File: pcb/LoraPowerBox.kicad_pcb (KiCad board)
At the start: 4 copper layers, 51.6 x 60.6 mm, 49 parts, among them J1 Conn_01x04_Pin, J10 Conn_01x02_Pin, J11 Conn_01x02_Pin, J12 Conn_01x05_Pin, J2 Conn_01x04_Pin, J3 Conn_01x04_Pin, J4 Conn_01x06_Pin, J5 Conn_01x04_Pin, J6 Conn_01x04_Pin, J7 Conn_01x04_Pin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

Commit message: pcb, sch: add resistor values for NTC voltage divider
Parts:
- R7: value R -> 5.23k
- R8: value R -> 30.1k
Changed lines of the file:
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@@
 			)
 		)
-		(property "Value" "R"
+		(property "Value" "5.23k"
 			(at 0 1.43 0)
 			(layer "F.Fab")
@@
 			)
 		)
-		(property "Value" "R"
+		(property "Value" "30.1k"
 			(at 0 1.43 0)
 			(layer "F.Fab")

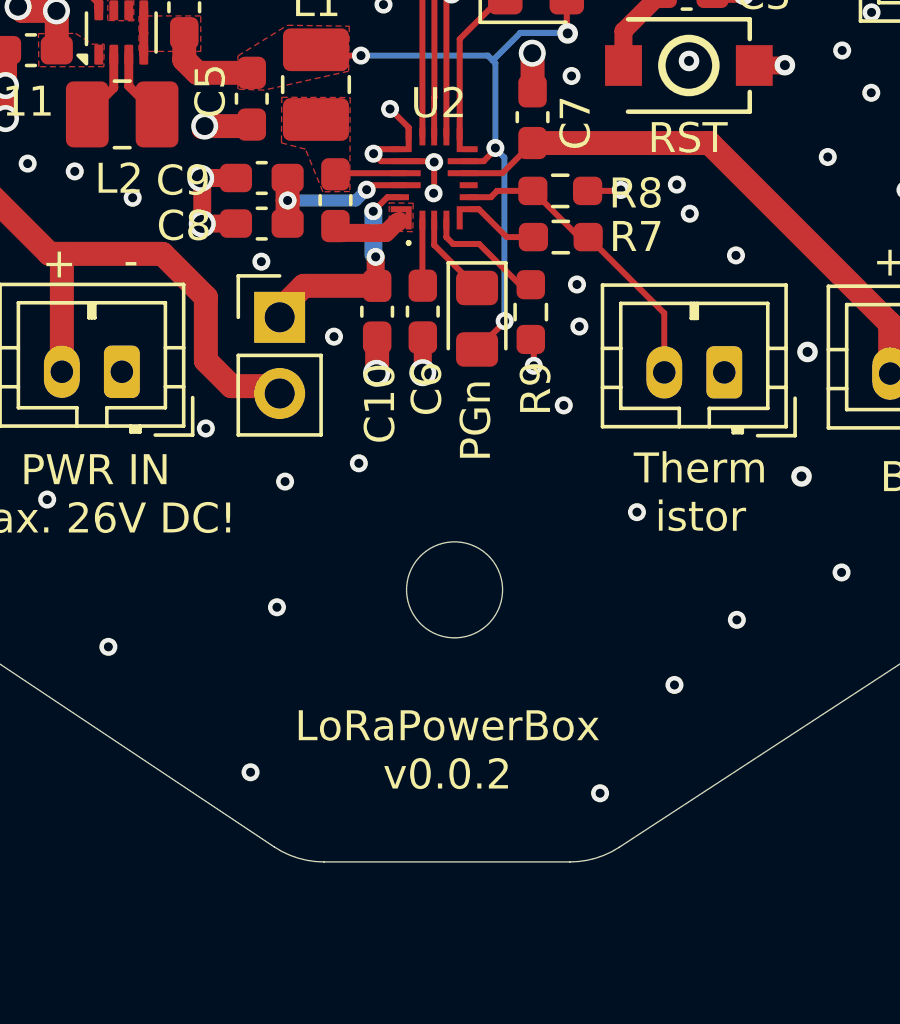
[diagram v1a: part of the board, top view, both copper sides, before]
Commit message: pcb, sch: replace M3 hounting hole with M4
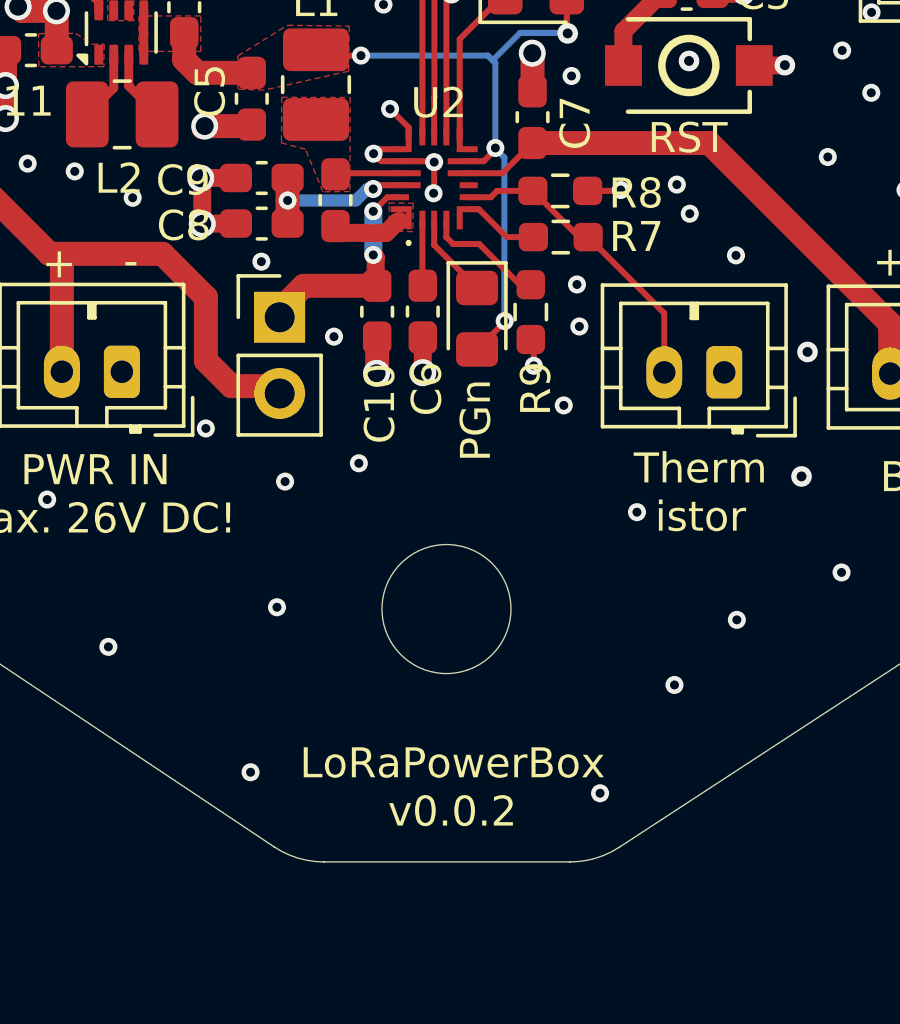
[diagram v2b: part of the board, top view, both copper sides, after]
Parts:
- H1: footprint MountingHole:MountingHole_3.2mm_M3 -> MountingHole:MountingHole_4.3mm_M4_DIN965
- moved H1 0.69 mm to (137.5, 91.6)
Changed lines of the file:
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@@
 		)
 	)
-	(footprint "MountingHole:MountingHole_3.2mm_M3"
+	(footprint "MountingHole:MountingHole_4.3mm_M4_DIN965"
 		(layer "F.Cu")
-		(at 137.76 90.93)
-		(descr "Mounting Hole 3.2mm, M3, no annular, generated by kicad-footprint-generator mountinghole.py")
-		(tags "mountinghole M3")
+		(at 137.49 91.57)
+		(descr "Mounting Hole 4.3mm, M4, no annular, generated by kicad-footprint-generator mountinghole.py")
+		(tags "mountinghole M4 DIN965")
 		(property "Reference" "H1"
-			(at 0 -4.15 0)
+			(at 0 -4.7 0)
 			(layer "F.SilkS")
 			(hide yes)
@@
 		)
 		(property "Value" "MountingHole"
-			(at 0 4.15 0)
+			(at 0 4.7 0)
 			(layer "F.Fab")
 			(hide yes)
@@
 		(fp_circle
 			(center 0 0)
-			(end 3.2 0)
+			(end 3.75 0)
 			(stroke
 				(width 0.15)
@@
 		(fp_circle
 			(center 0 0)
-			(end 3.45 0)
+			(end 4 0)
 			(stroke
 				(width 0.05)
@@
 		)
 		(fp_text user "${REFERENCE}"
-			(at -0.168654 0.2 0)
+			(at 0 0 0)
 			(layer "F.Fab")
 			(effects
@@
 		(pad "" np_thru_hole circle
 			(at 0 0)
-			(size 3.2 3.2)
-			(drill 3.2)
+			(size 4.3 4.3)
+			(drill 4.3)
 			(layers "*.Cu" "*.Mask")
 		)
@@
 	)
 	(gr_text "LoRaPowerBox\nv0.0.2\n"
-		(at 137.525 97.675 0)
+		(at 137.69 98.91 0)
 		(layer "F.SilkS")
 		(effects
@@
 	)
 	(segment
+		(start 135.04771 77.56825)
+		(end 135.17471 77.44125)
+		(width 0.2)
+		(layer "F.Cu")
+		(net 7)
+	)
+	(segment
 		(start 132.195 77.95125)
 		(end 132.195 77.20125)
@@
 	)
 	(segment
-		(start 134.83 77.59125)
-		(end 134.98 77.44125)
+		(start 135.17471 77.44125)
+		(end 136.13 77.44125)
 		(width 0.2)
 		(layer "F.Cu")
@@
 		(net 7)
 	)
-	(segment
-		(start 134.98 77.44125)
-		(end 136.13 77.44125)
-		(width 0.2)
-		(layer "F.Cu")
-		(net 7)
-	)
 	(via
 		(at 132.195 77.95125)
@@
 	)
 	(via
-		(at 134.83 77.59125)
+		(at 135.04771 77.56825)
 		(size 0.6)
 		(drill 0.3)
@@
 	)
 	(segment
-		(start 134.83 77.59125)
+		(start 135.04771 77.56825)
+		(end 134.853 77.56825)
+		(width 0.4)
+		(layer "B.Cu")
+		(net 7)
+	)
+	(segment
+		(start 134.853 77.56825)
 		(end 134.47 77.95125)
 		(width 0.4)
@@
 	)
 	(segment
-		(start 135.13 79.83125)
-		(end 135.13 80.74625)
-		(width 0.6)
-		(layer "F.Cu")
-		(net 9)
-	)
-	(segment
 		(start 132.73375 80.79625)
 		(end 131.93 81.6)
@@
 		(net 9)
 	)
+	(segment
+		(start 135.13 79.84625)
+		(end 135.13 80.74625)
+		(width 0.6)
+		(layer "F.Cu")
+		(net 9)
+	)
+	(segment
+		(start 135.05 79.76625)
+		(end 135.13 79.84625)
+		(width 0.6)
+		(layer "F.Cu")
+		(net 9)
+	)
 	(via
-		(at 135.13 79.83125)
+		(at 135.05 79.76625)
 		(size 0.6)
 		(drill 0.3)
@@
 	(segment
 		(start 135.05 79.75125)
-		(end 135.13 79.83125)
+		(end 135.05 79.76625)
 		(width 0.2)
 		(layer "B.Cu")

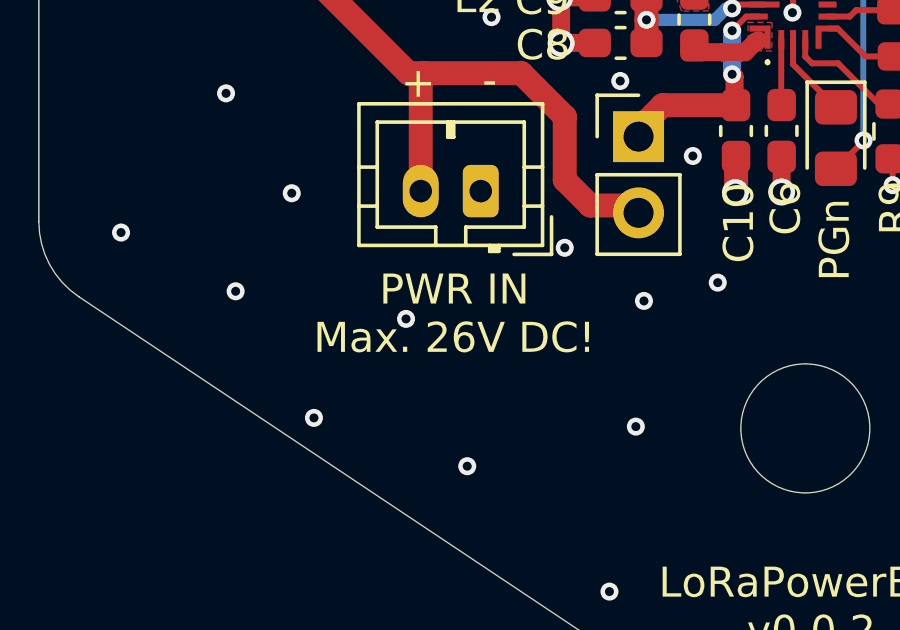
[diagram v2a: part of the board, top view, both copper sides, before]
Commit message: pcb: the internal ADC maxes out at 18V. So rework silk print regaring voltage limits
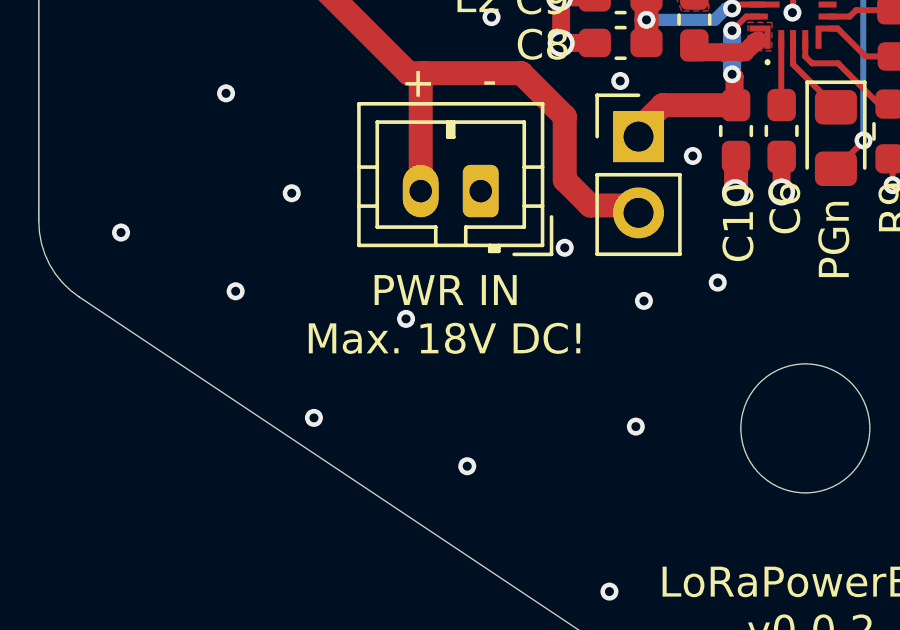
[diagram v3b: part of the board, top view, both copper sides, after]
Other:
- board text added: "PWR IN Max. 18V DC!"
- board text removed: "PWR IN Max. 26V DC!"
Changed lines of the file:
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@@
 		)
 	)
-	(gr_text "PWR IN\nMax. 26V DC!"
-		(at 125.79 89.14 0)
+	(gr_text "PWR IN\nMax. 18V DC!\n"
+		(at 125.5 89.19 0)
 		(layer "F.SilkS")
 		(effects

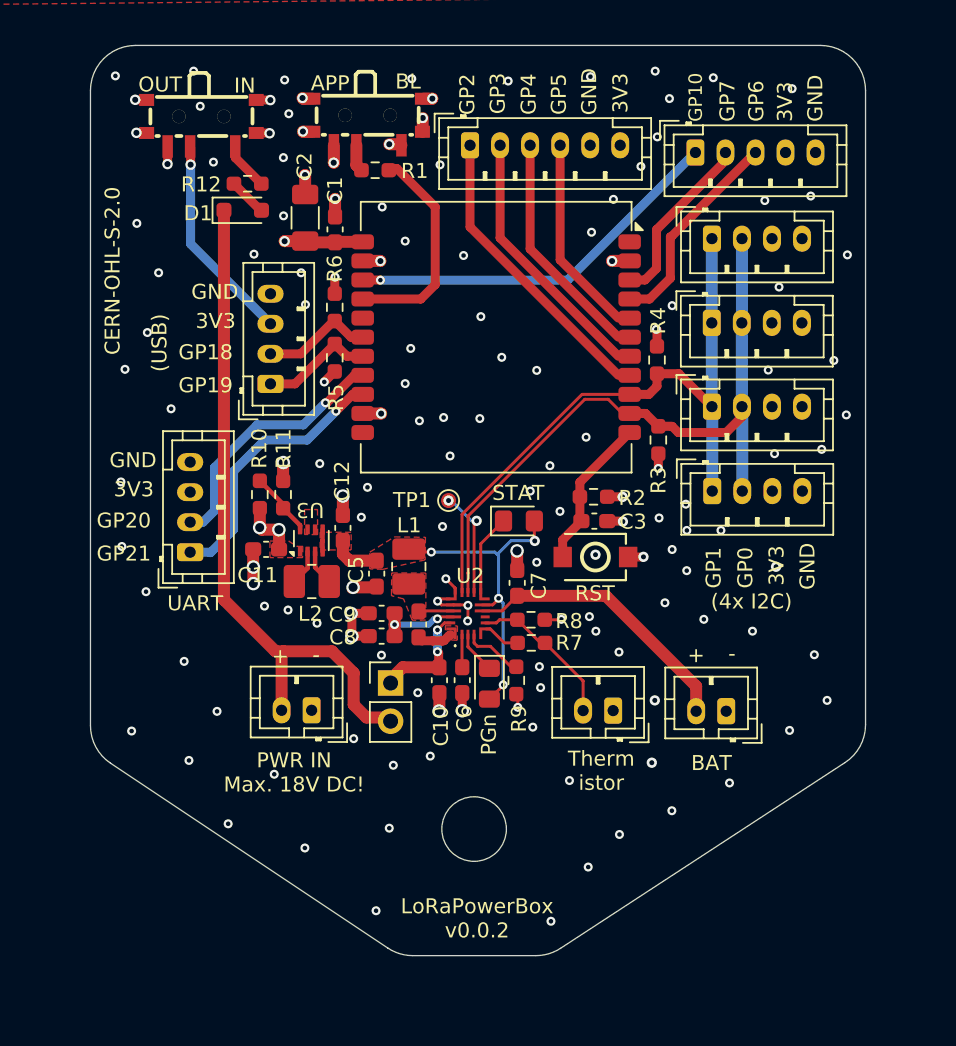
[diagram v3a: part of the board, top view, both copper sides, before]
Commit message: pcb: finally found the right kicad buttoms to center everything correctly
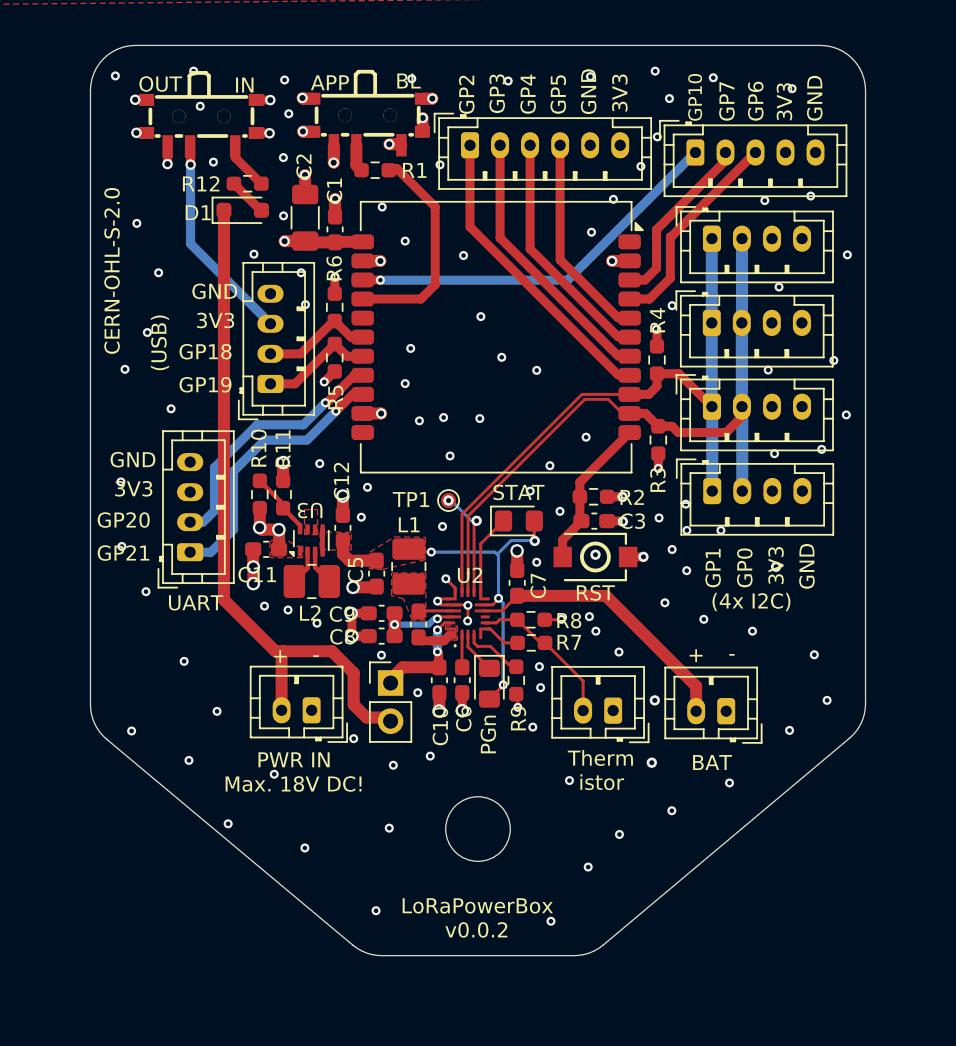
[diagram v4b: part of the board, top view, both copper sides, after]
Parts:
- moved H1 0.26 mm to (137.8, 91.6)
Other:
- outline, holes or cut-outs redrawn
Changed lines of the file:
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@@
 	(footprint "MountingHole:MountingHole_4.3mm_M4_DIN965"
 		(layer "F.Cu")
-		(at 137.49 91.57)
+		(at 137.75 91.57)
 		(descr "Mounting Hole 4.3mm, M4, no annular, generated by kicad-footprint-generator mountinghole.py")
 		(tags "mountinghole M4 DIN965")
@@
 	)
 	(gr_line
-		(start 143.247437 99.512001)
-		(end 162.200077 87.137889)
+		(start 160.56 39.38)
+		(end 114.94 39.38)
 		(stroke
-			(width 0.0381)
+			(width 0.05)
 			(type default)
 		)
@@
 	)
 	(gr_arc
-		(start 143.247437 99.512001)
-		(mid 142.462928 99.875403)
-		(end 141.60736 100)
+		(start 163.56 83.2276)
+		(mid 163.279144 84.494982)
+		(end 162.489113 85.525065)
 		(stroke
 			(width 0.0381)
@@
 		(layer "Edge.Cuts")
 	)
-	(gr_line
-		(start 160.56 39.38)
-		(end 114.94 39.38)
-		(stroke
-			(width 0.05)
-			(type default)
-		)
-		(layer "Edge.Cuts")
-	)
 	(gr_arc
-		(start 113.275749 87.18216)
-		(mid 112.294933 86.101603)
-		(end 111.94 84.686109)
+		(start 131.3392 100)
+		(mid 130.315387 99.819901)
+		(end 129.414513 99.301226)
 		(stroke
 			(width 0.0381)
@@
 	)
 	(gr_line
-		(start 163.56 84.625888)
+		(start 163.56 83.2276)
 		(end 163.56 42.38)
 		(stroke
@@
 		(layer "Edge.Cuts")
 	)
-	(gr_arc
-		(start 163.56 84.625888)
-		(mid 163.198203 86.054133)
-		(end 162.200077 87.137889)
-		(stroke
-			(width 0.05)
-			(type default)
-		)
-		(layer "Edge.Cuts")
-	)
 	(gr_line
-		(start 133.408426 100)
-		(end 141.60736 100)
+		(start 131.3392 100)
+		(end 144.167198 100)
 		(stroke
 			(width 0.0381)
-			(type default)
+			(type solid)
 		)
 		(layer "Edge.Cuts")
@@
 	(gr_line
 		(start 111.94 42.38)
-		(end 111.94 84.686109)
+		(end 111.94 83.2842)
 		(stroke
 			(width 0.05)
@@
 		(layer "Edge.Cuts")
 	)
-	(gr_line
-		(start 131.744175 99.496051)
-		(end 113.275749 87.18216)
+	(gr_arc
+		(start 146.086717 99.297446)
+		(mid 145.184055 99.81891)
+		(end 144.167198 100)
 		(stroke
 			(width 0.0381)
@@
 	)
 	(gr_arc
+		(start 113.015352 85.585495)
+		(mid 112.222112 84.554287)
+		(end 111.940039 83.2842)
+		(stroke
+			(width 0.05)
+			(type default)
+		)
+		(layer "Edge.Cuts")
+	)
+	(gr_arc
 		(start 160.56 39.38)
 		(mid 162.68132 40.25868)
@@
 		(layer "Edge.Cuts")
 	)
-	(gr_arc
-		(start 133.408426 100)
-		(mid 132.538984 99.871257)
-		(end 131.744175 99.496051)
+	(gr_line
+		(start 146.086717 99.297446)
+		(end 162.489113 85.525065)
+		(stroke
+			(width 0.0381)
+			(type default)
+		)
+		(layer "Edge.Cuts")
+	)
+	(gr_line
+		(start 129.414513 99.301226)
+		(end 113.015352 85.585498)
 		(stroke
 			(width 0.0381)

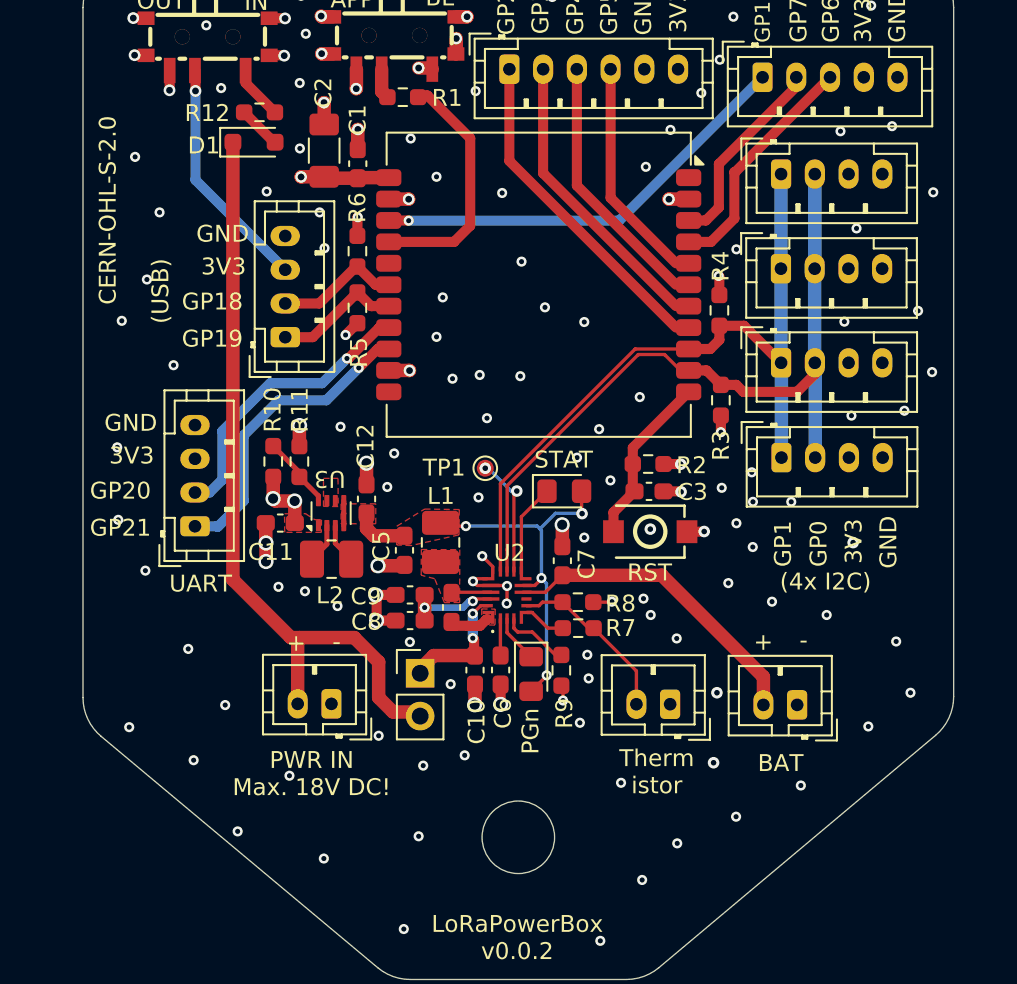
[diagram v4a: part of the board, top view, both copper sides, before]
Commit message: sch, pcb: add reset IC that monitors the battery for us
The BQ25628 has a UVLO (Battery Undervoltage Lockout) protection which
is very very low (configurable voltages <2.5).

Add an additional battery monitor which allows us to automatically
switch off the 3.3V coming from the Buck-/Boost-Converter but keeps the
BQ25628 alive so it can recharge the battery.
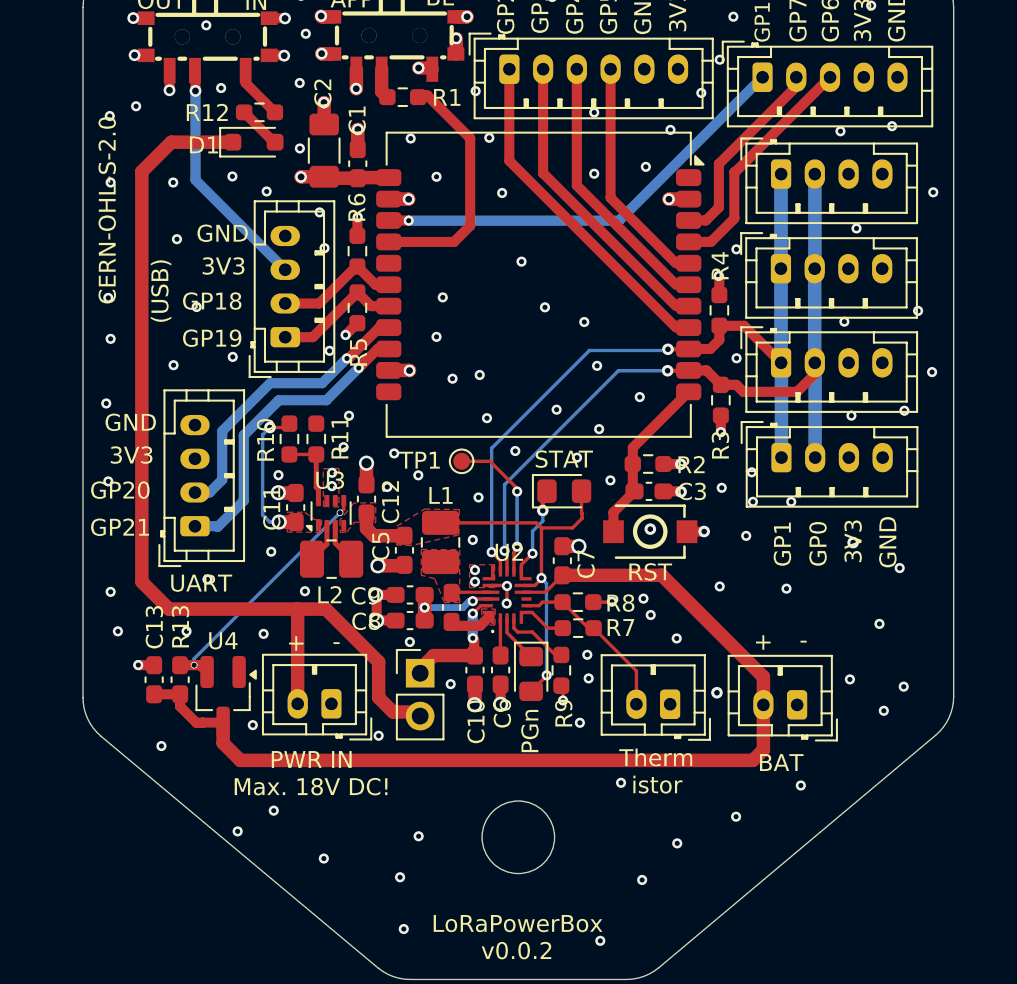
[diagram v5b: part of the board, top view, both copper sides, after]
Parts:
- added C13: 100nF, Capacitor_SMD:C_0603_1608Metric_Pad1.08x0.95mm_HandSolder, F.Cu at (116.2, 82.2)
- added R13: 100k, Capacitor_SMD:C_0603_1608Metric_Pad1.08x0.95mm_HandSolder, F.Cu at (117.7, 82.2)
- added U4: APX803L05, Package_TO_SOT_SMD:SOT-23_Handsoldering, F.Cu at (120.2, 83.3)
- moved R11 1.67 mm to (125.8, 68.0)
- moved R10 1.64 mm to (124.2, 68.0), turned to -90 degrees
- moved TP1 1.46 mm to (134.4, 69.3)
- moved C11 1.30 mm to (124.5, 72.0), turned to 90 degrees
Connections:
- net Net-(J10-Pin_2) renamed /VBAT
- U3 pad 5: /SYS -> Net-(U3-EN)
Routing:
- net /VBAT: track 18.8 -> 60.6 mm
- net Net-(U3-EN): track 0.00 -> 15.2 mm, vias 0 -> 2
- net /VBUS: track 45.5 -> 57.0 mm
- net GND: track 36.4 -> 31.7 mm, vias 139 -> 155
- net +3V3: track 16.6 -> 21.1 mm
- net /I2C1_SCK: track 43.5 -> 45.4 mm, vias 0 -> 2
- net Net-(U2-INTn): track 7.28 -> 8.96 mm
- net /SYS: track 26.3 -> 25.2 mm, vias 4 -> 2
- net Net-(D2-K): track 5.51 -> 5.15 mm, vias 0 -> 2
- net /I2C1_SCL: track 44.9 -> 44.8 mm, vias 0 -> 2
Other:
- board text removed: "(4x I2C)"
